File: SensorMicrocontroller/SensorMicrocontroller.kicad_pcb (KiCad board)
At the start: 2 copper layers, 100 x 100 mm, 41 parts, among them J1 JST B4B-PH-SM4-TB, J2 JST B4B-PH-SM4-TB, J3 JST B6B-PH-SM4-TB, J4 JST B4B-PH-SM4-TB, J5 JST B4B-PH-SM4-TB, J8 12V Connector, J9 Light Connector, Q1 DMT6009LCT, Q2 DMT6009LCT, U1 ADS1115IDGS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

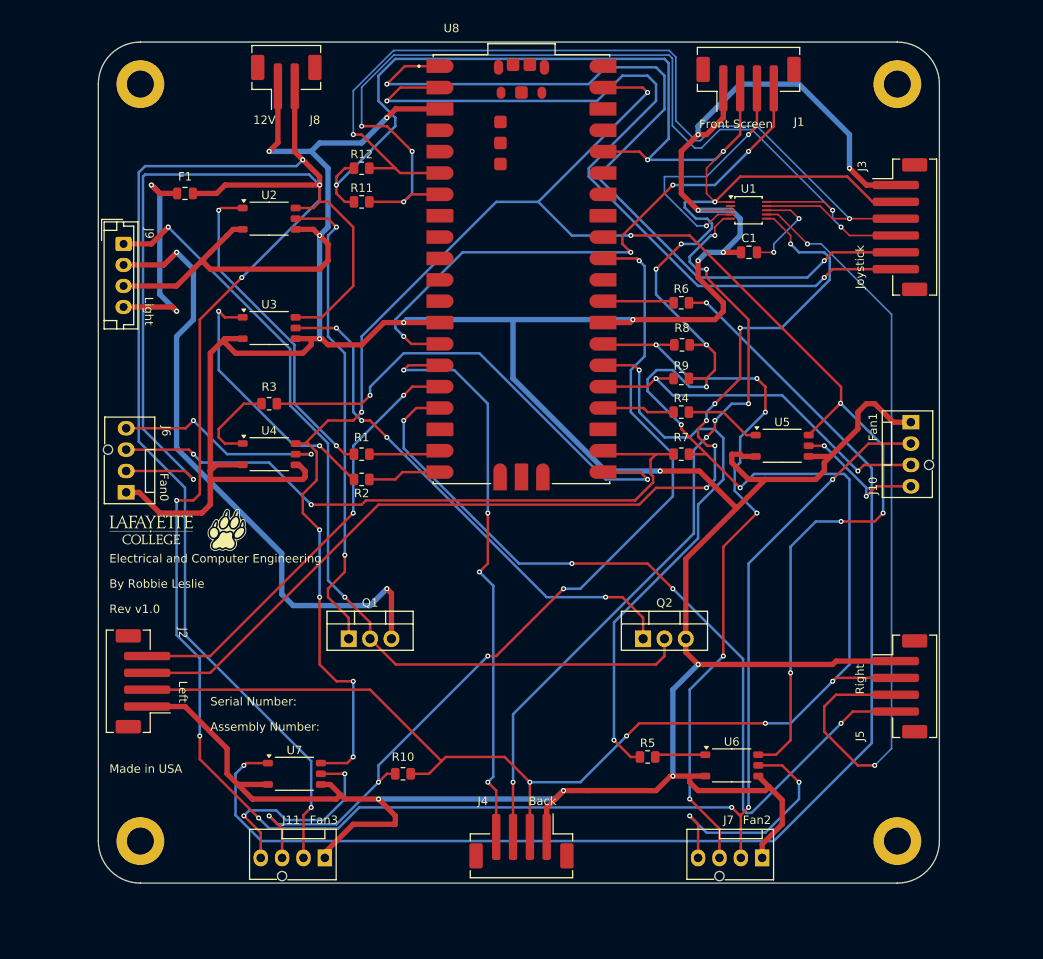
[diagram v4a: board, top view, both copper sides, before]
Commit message: Added fill zone
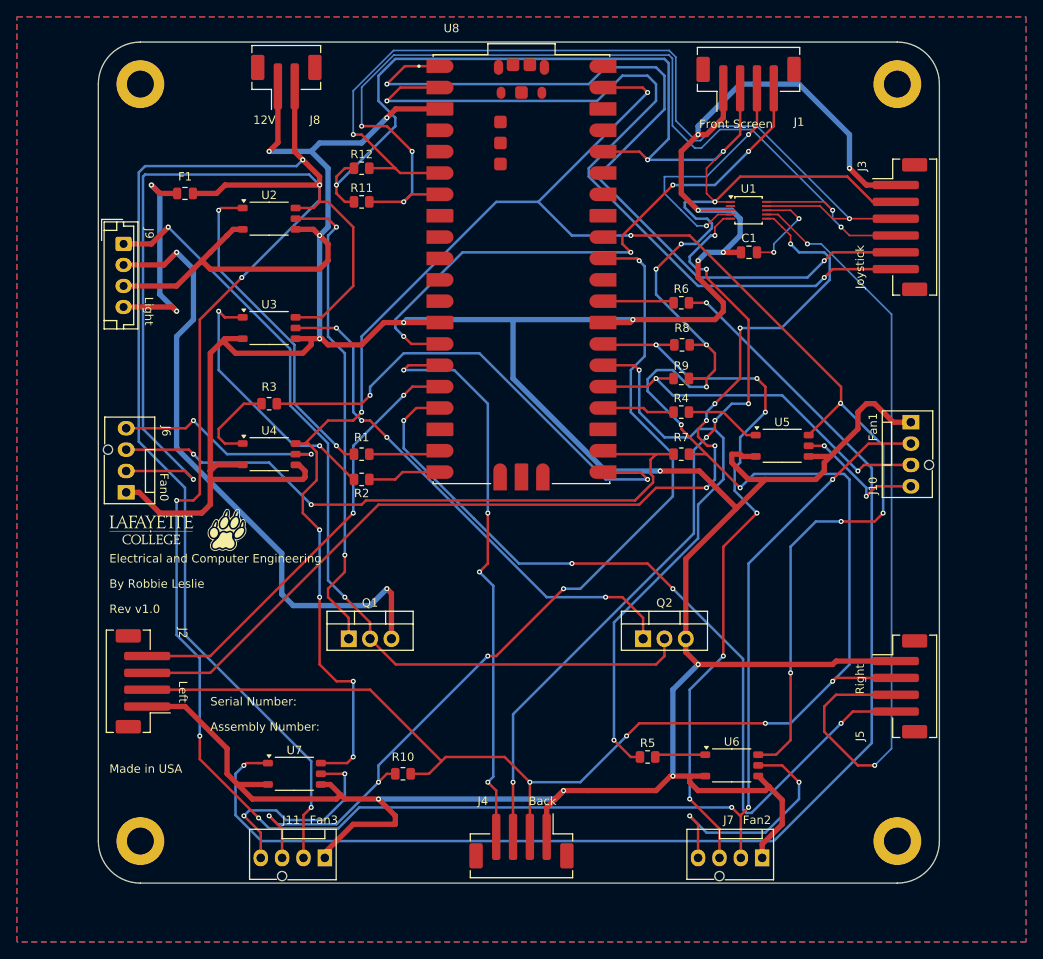
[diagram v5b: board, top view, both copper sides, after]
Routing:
- added copper zone on B.Cu, net /GND
- added copper zone on F.Cu, net /GND
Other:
- board text added: "2/2/25"
- board text removed: "2/1/25"
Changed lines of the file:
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@@
 		)
 	)
-	(gr_text "2/1/25"
+	(gr_text "2/2/25"
 		(at 206 194 0)
 		(layer "Cmts.User")
@@
 		(net 73)
 	)
+	(zone
+		(net 2)
+		(net_name "/GND")
+		(layers "F&B.Cu")
+		(hatch edge 0.5)
+		(connect_pads
+			(clearance 0.5)
+		)
+		(min_thickness 0.25)
+		(filled_areas_thickness no)
+		(fill yes
+			(thermal_gap 0.5)
+			(thermal_bridge_width 0.5)
+		)
+		(polygon
+			(pts
+				(xy 85 45) (xy 205 45) (xy 205 155) (xy 85 155)
+			)
+		)
+	)
 )

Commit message: Started re-route
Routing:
- net /GND: track 560.7 -> 0.00 mm, vias 16 -> 0
- net /3.3V: track 343.7 -> 0.00 mm, vias 14 -> 0
- net /5V: track 224.3 -> 0.00 mm, vias 11 -> 0
- net Net-(U7-Anode): track 153.6 -> 0.00 mm, vias 2 -> 0
- net /US2: track 124.1 -> 0.00 mm, vias 6 -> 0
- net /SCL: track 116.4 -> 0.00 mm, vias 5 -> 0
- net /SDA: track 111.6 -> 0.00 mm, vias 2 -> 0
- net /Fan Sense3: track 109.2 -> 0.00 mm, vias 5 -> 0
- net /PIR3: track 100.2 -> 0.00 mm, vias 4 -> 0
- net /RXFinger: track 98.5 -> 0.00 mm, vias 2 -> 0
- net /TXFinger: track 97.7 -> 0.00 mm, vias 2 -> 0
- net /US3: track 94.0 -> 0.00 mm, vias 2 -> 0
- net /US1: track 92.6 -> 0.00 mm, vias 6 -> 0
- net /Fan Sense2: track 87.0 -> 0.00 mm, vias 6 -> 0
- net /Fan Sense0: track 78.8 -> 0.00 mm, vias 2 -> 0
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
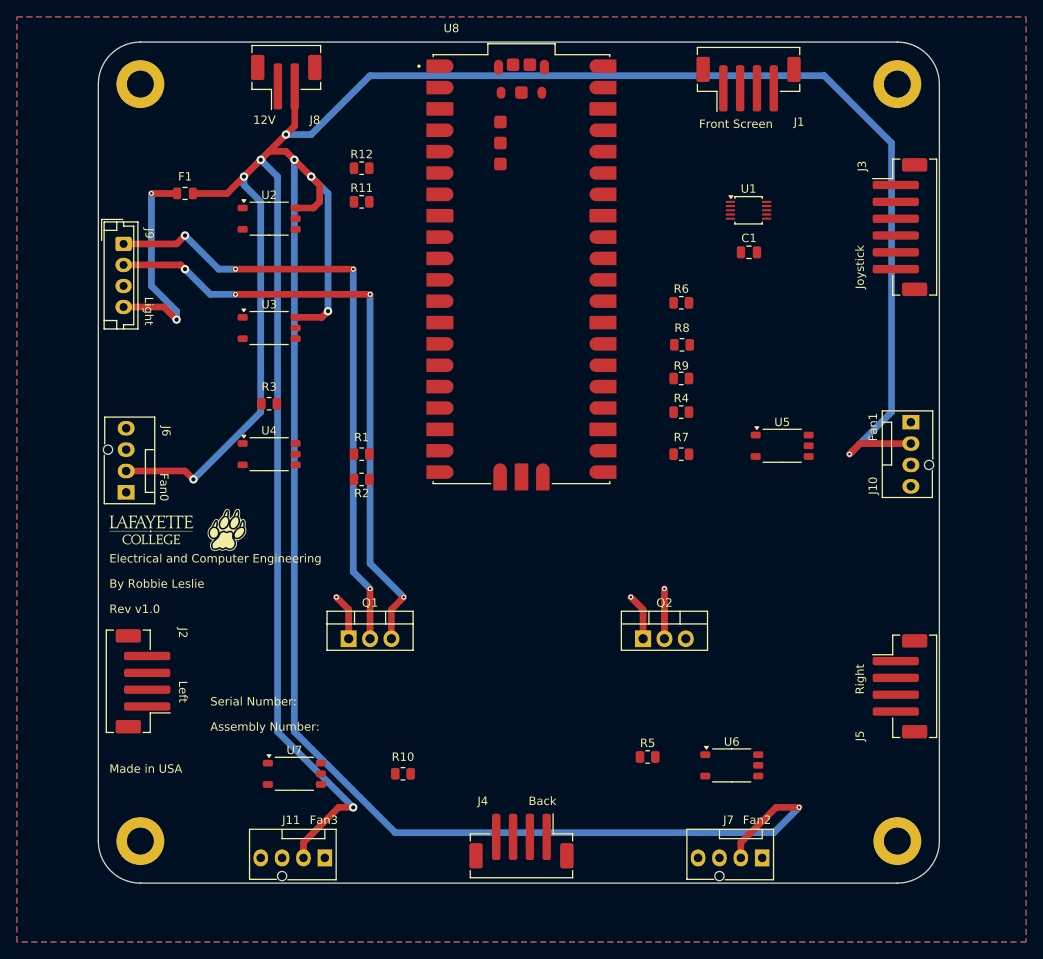
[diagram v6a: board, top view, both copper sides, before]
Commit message: Continued re-routing traces
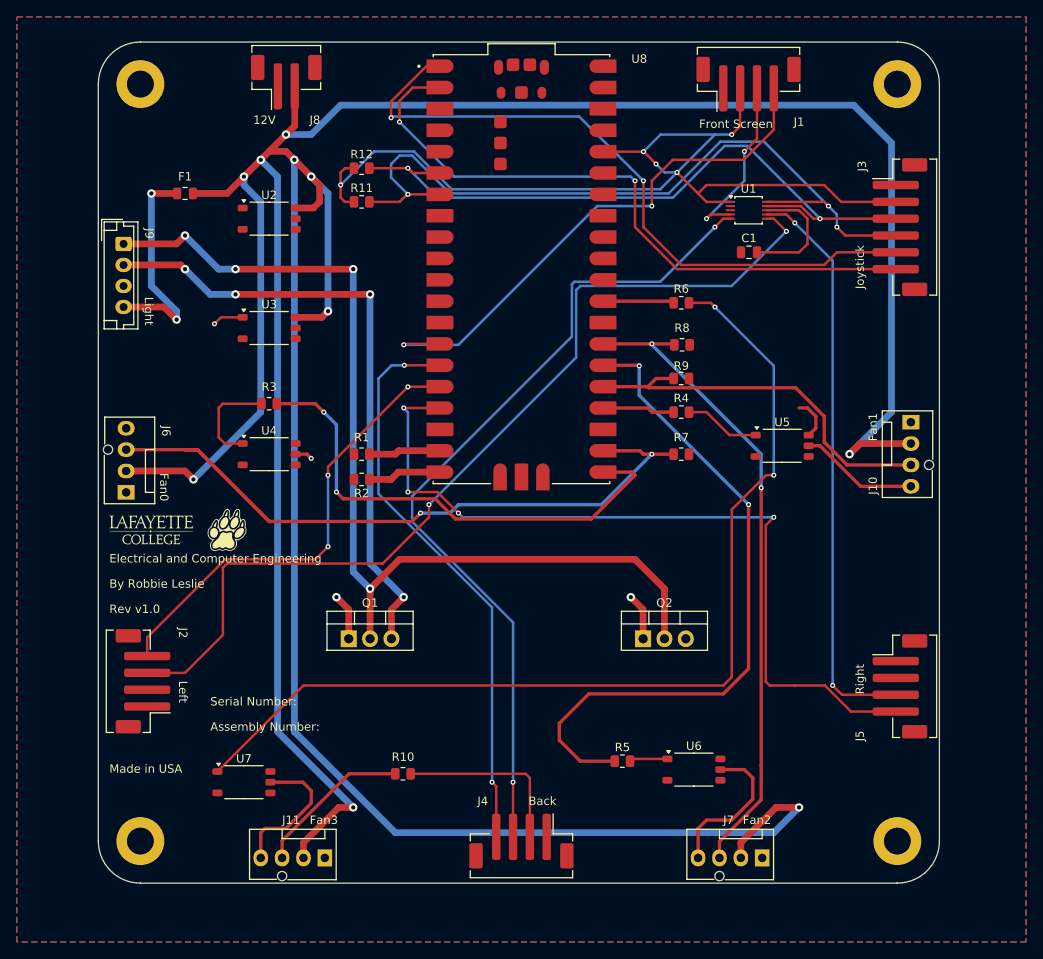
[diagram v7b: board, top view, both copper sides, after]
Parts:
- moved U7 6.08 mm to (112.0, 136.0)
- moved U6 4.53 mm to (165.5, 134.5)
- moved R5 3.04 mm to (157.0, 133.5)
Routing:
- net /3.3V: track 0.00 -> 138.3 mm, vias 0 -> 5
- net Net-(U7-Anode): track 0.00 -> 118.6 mm, vias 0 -> 2
- net /US2: track 0.00 -> 111.0 mm, vias 0 -> 2
- net /US1: track 0.00 -> 100.6 mm, vias 0 -> 2
- net /PIR3: track 0.00 -> 96.1 mm, vias 0 -> 4
- net /Fan Sense0: track 0.00 -> 91.4 mm, vias 0 -> 2
- net /SCL: track 0.00 -> 91.1 mm, vias 0 -> 3
- net /SDA: track 0.00 -> 81.2 mm, vias 0 -> 2
- net /RXFinger: track 0.00 -> 80.7 mm, vias 0 -> 2
- net /PWM2 3.3V: track 0.00 -> 80.5 mm, vias 0 -> 2
- net /TXFinger: track 0.00 -> 77.4 mm, vias 0 -> 2
- net /Fan Sense2: track 0.00 -> 77.0 mm, vias 0 -> 2
- net /US3: track 0.00 -> 68.6 mm, vias 0 -> 2
- net /PIR1: track 0.00 -> 68.4 mm, vias 0 -> 2
- net /PIR0: track 0.00 -> 65.6 mm, vias 0 -> 2
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
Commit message: Finished re-route
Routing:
- net /5V: track 5.00 -> 262.3 mm, vias 0 -> 5
- net /3.3V: track 138.3 -> 336.8 mm, vias 5 -> 14
- net /Fan Sense3: track 18.8 -> 121.2 mm, vias 0 -> 2
- net /GND: track 0.00 -> 85.7 mm, vias 0 -> 35
- net /Light On 2: track 5.55 -> 78.4 mm, vias 1 -> 2
- net Net-(U2-Anode): track 0.00 -> 63.4 mm
- net /Light On 1: track 5.55 -> 65.3 mm, vias 1 -> 2
- net /PWM0 5V: track 2.06 -> 35.6 mm, vias 1 -> 0
- net Net-(U3-Anode): track 3.67 -> 26.8 mm, vias 1 -> 0
- net /Fan Sense0: track 91.4 -> 77.9 mm
- net /PWM0 3.3V: track 59.1 -> 51.9 mm
- net /US1: track 100.6 -> 106.0 mm
- net /PIR2: track 54.9 -> 57.0 mm, vias 3 -> 2
- net /PIR3: track 96.1 -> 98.0 mm
- net /SDA: track 81.2 -> 82.1 mm
